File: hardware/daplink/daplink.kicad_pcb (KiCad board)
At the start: 2 copper layers, 50 x 20 mm, 35 parts, among them J1 Conn_01x04, J2 Conn_01x05, J3 Conn_01x05, P1 USB_C_Receptacle_USB2.0, U1 AMS1117-3.3, U2 STM32F103CBTx, Y1 8MHz

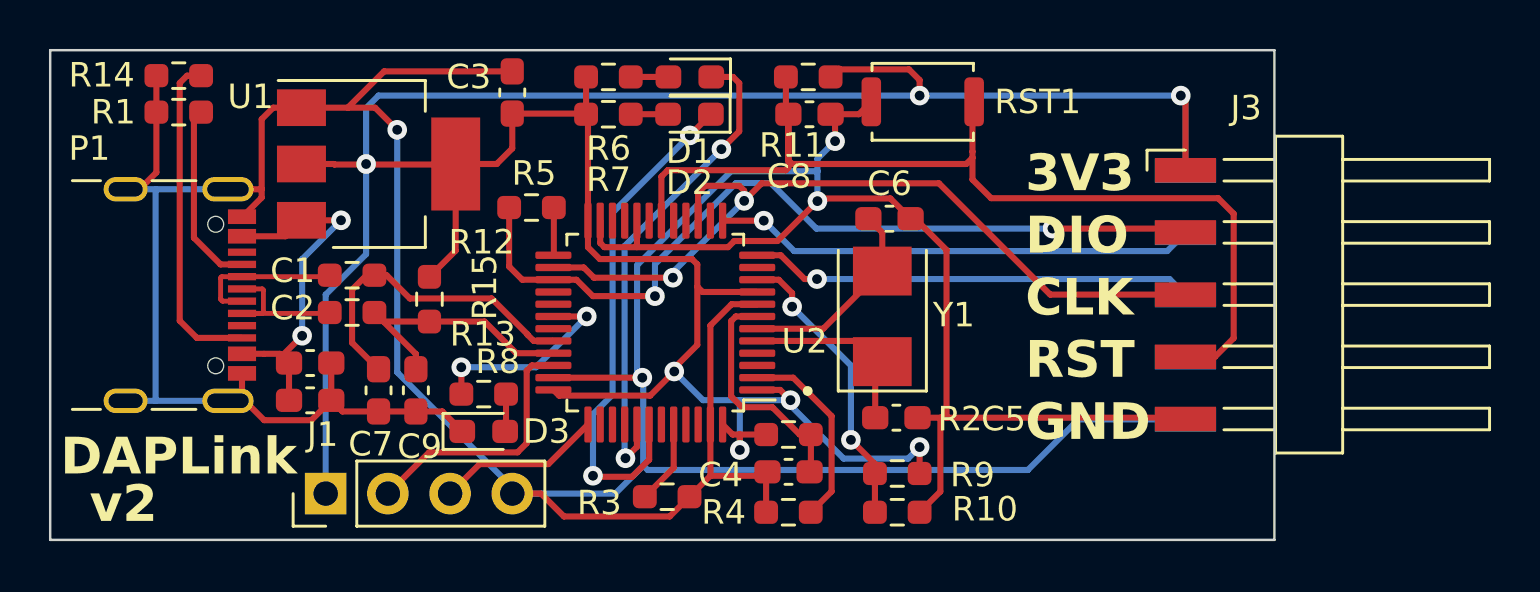
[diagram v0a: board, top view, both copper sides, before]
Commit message: refactor(hw/usb): modify board outline
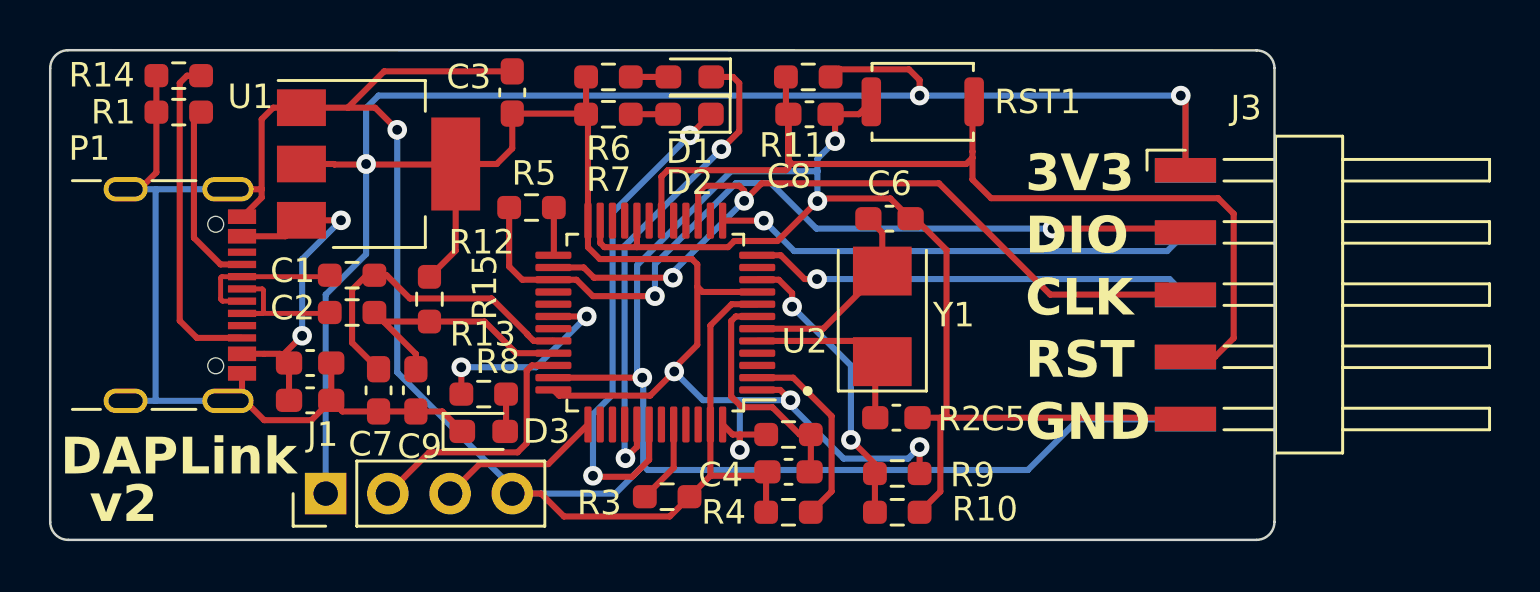
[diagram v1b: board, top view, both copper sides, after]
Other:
- outline, holes or cut-outs redrawn
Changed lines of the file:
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@@
   (gr_circle (center 130.937 113.919) (end 131.064 113.919)
     (stroke (width 0.15) (type solid)) (fill solid) (layer "F.SilkS"))
-  (gr_line (start 100 120) (end 150 120)
+  (gr_line (start 100.7364 120) (end 149.277247 120)
     (stroke (width 0.1) (type default)) (layer "Edge.Cuts"))
-  (gr_line (start 150 120) (end 150 100)
+  (gr_arc (start 150.001351 119.2636) (mid 149.79 119.779985) (end 149.277247 120)
     (stroke (width 0.1) (type default)) (layer "Edge.Cuts"))
-  (gr_line (start 100 100) (end 100 120)
+  (gr_line (start 150.001351 119.2636) (end 150.003816 100.732769)
     (stroke (width 0.1) (type default)) (layer "Edge.Cuts"))
-  (gr_line (start 150 100) (end 100 100)
+  (gr_line (start 100 100.7364) (end 100 119.275896)
+    (stroke (width 0.1) (type default)) (layer "Edge.Cuts"))
+  (gr_line (start 149.267416 100.008665) (end 100.724104 100)
+    (stroke (width 0.1) (type default)) (layer "Edge.Cuts"))
+  (gr_arc (start 100 100.7364) (mid 100.211351 100.220015) (end 100.724104 100)
+    (stroke (width 0.1) (type default)) (layer "Edge.Cuts"))
+  (gr_arc (start 149.267416 100.008665) (mid 149.7838 100.220016) (end 150.003816 100.732769)
+    (stroke (width 0.1) (type default)) (layer "Edge.Cuts"))
+  (gr_arc (start 100.7364 120) (mid 100.220015 119.788649) (end 100 119.275896)
     (stroke (width 0.1) (type default)) (layer "Edge.Cuts"))
   (gr_text "GND" (at 144.569856 116.06) (layer "B.SilkS")
